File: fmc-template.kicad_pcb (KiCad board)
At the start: 6 copper layers, 84 x 69 mm, 40 parts, among them J19 WP Jumper, P1 ASP-134488-01, Q1 FDN335N, Q2 FDN335N, Q3 FDN335N, U9 AT24C64D

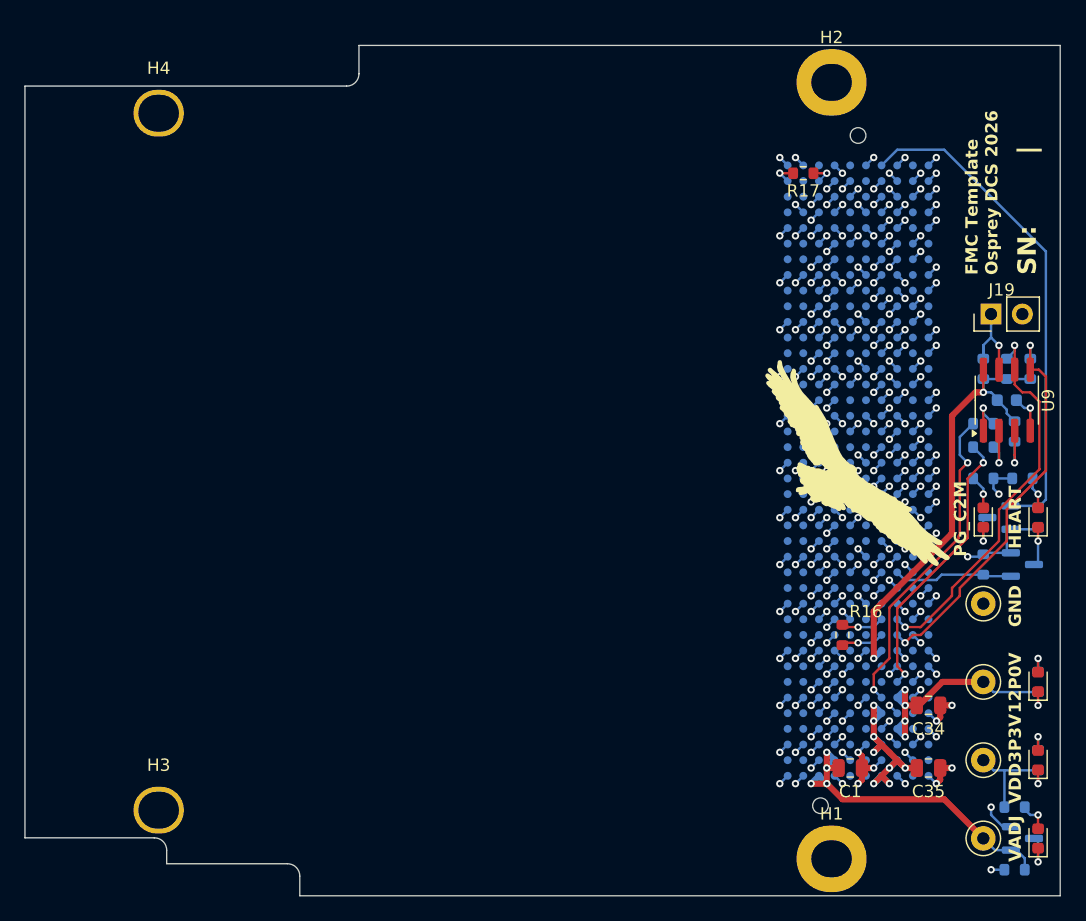
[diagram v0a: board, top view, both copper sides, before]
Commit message: Changed 22uF to 1210
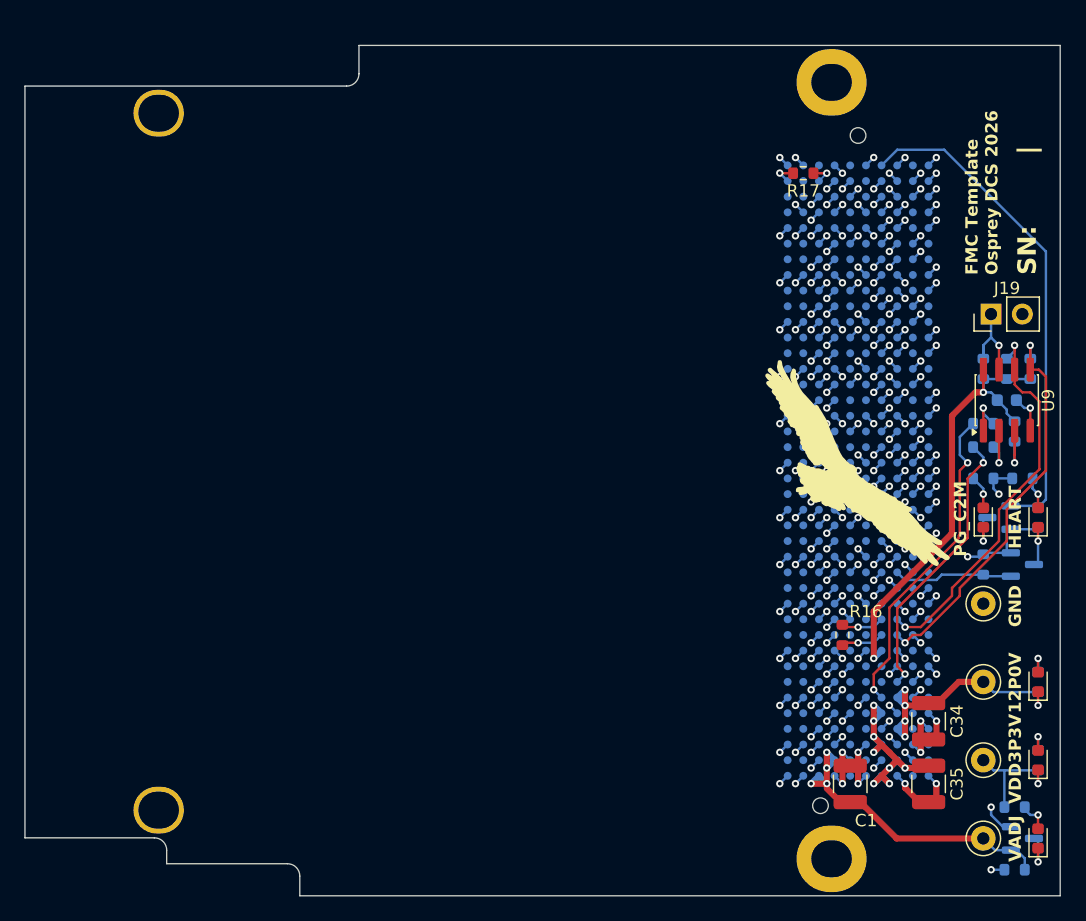
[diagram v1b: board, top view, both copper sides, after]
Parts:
- C1, C34, C35: footprint Capacitor_SMD:C_0805_2012Metric -> Capacitor_SMD:C_1210_3225Metric
- moved C34 1.29 mm to (180.3, 125.8), turned to -90 degrees
- moved C35 1.29 mm to (180.3, 130.9), turned to -90 degrees
- moved C1 1.29 mm to (174.0, 130.9), turned to 90 degrees
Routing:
- net GND: track 171.6 -> 179.7 mm, vias 168 -> 166
- net VADJ: track 29.1 -> 28.4 mm
- net 12P0V: track 20.0 -> 19.4 mm
